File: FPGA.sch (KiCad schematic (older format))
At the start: 32 parts, among them P3 CONN_02X22, P4 CONN_02X22, SW1 SW_PUSH, U6 ICE40HX1K-VQ100, X2 IQXO/7X

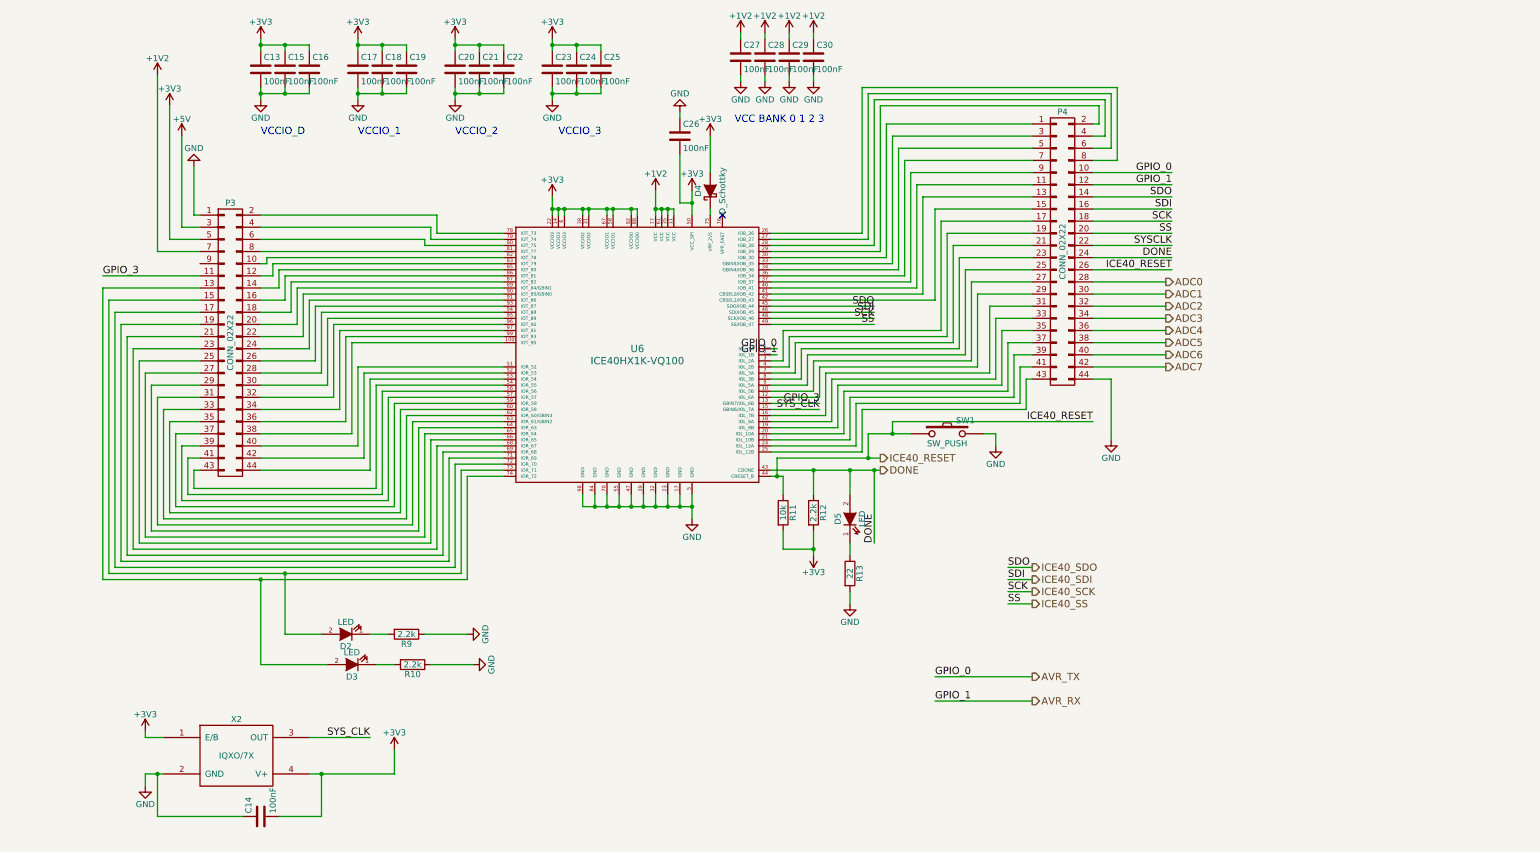
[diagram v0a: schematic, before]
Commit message: Redesign FPGA <-> connectors
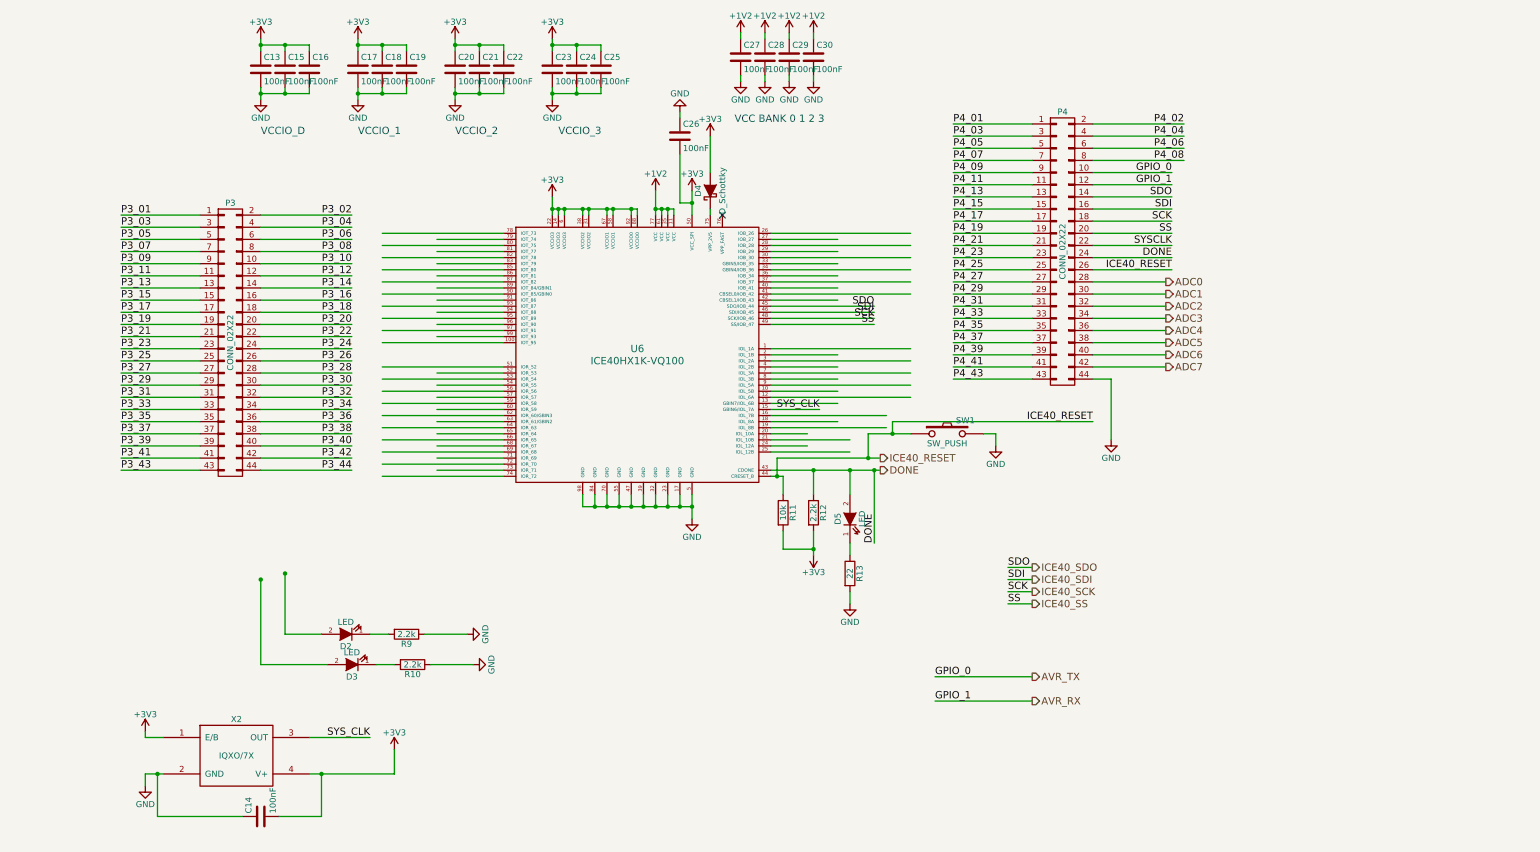
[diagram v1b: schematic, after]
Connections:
- net labels added: P3_01, P3_02, P3_03, P3_04, P3_05, P3_06, P3_07, P3_08, P3_09, P3_10, P3_11, P3_12, P3_13, P3_14, P3_15, P3_16, P3_17, P3_18, P3_19, P3_20, P3_21, P3_22, P3_23, P3_24, P3_25, P3_26, P3_27, P3_28, P3_29, P3_30, P3_31, P3_32, P3_33, P3_34, P3_35, P3_36, P3_37, P3_38, P3_39, P3_40, P3_41, P3_42, P3_43, P3_44, P4_01, P4_02, P4_03, P4_04, P4_05, P4_06, P4_07, P4_08, P4_09, P4_11, P4_13, P4_15, P4_17, P4_19, P4_21, P4_23, P4_25, P4_27, P4_29, P4_31, P4_33, P4_35, P4_37, P4_39, P4_41, P4_43
- net labels removed: +5V, GPIO_3
- wire segments 411 -> 278

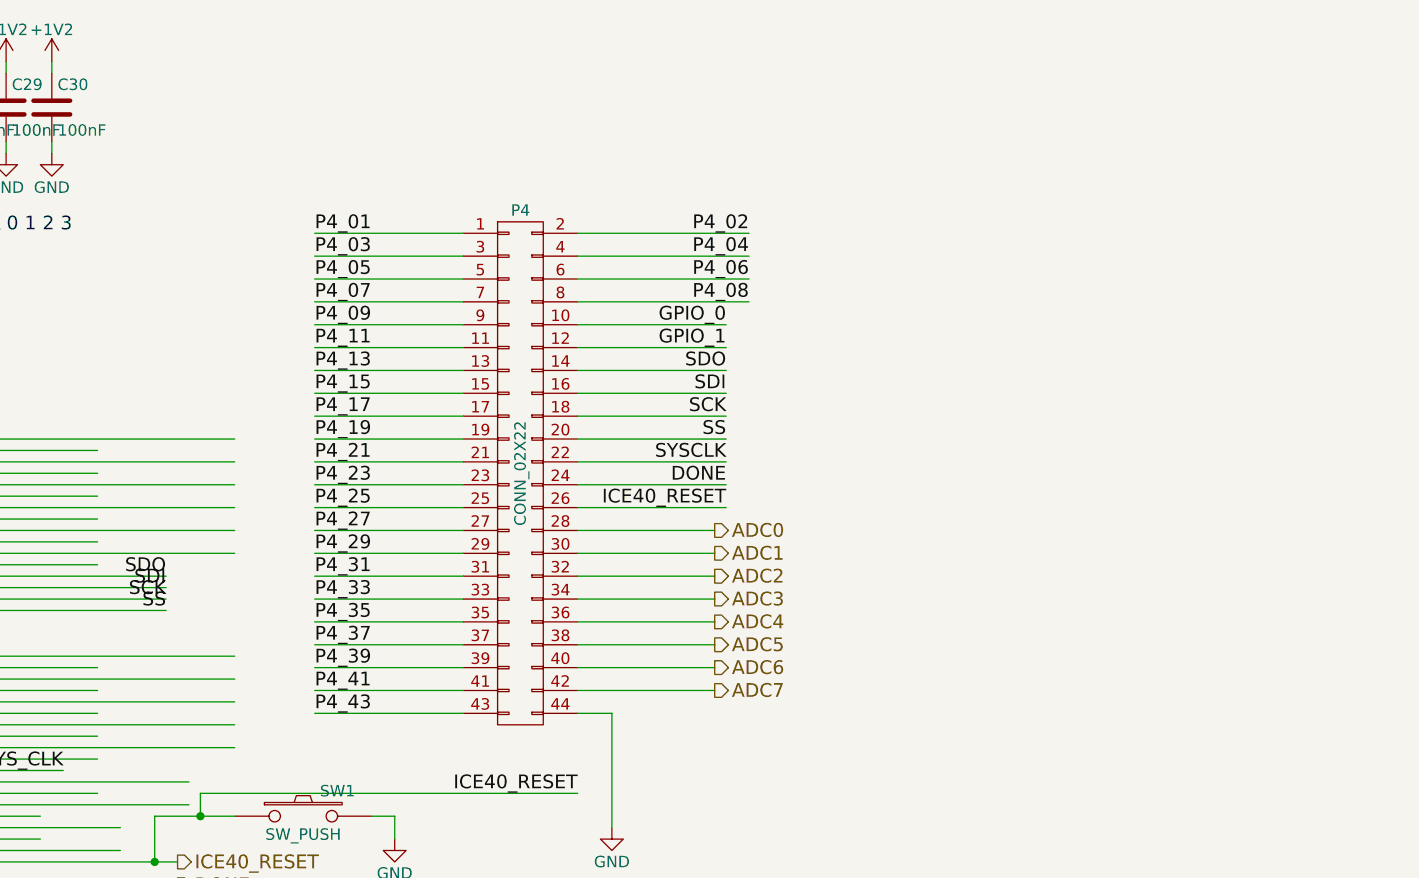
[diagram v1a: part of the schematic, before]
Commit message: Reorder conectors <-> FPGA
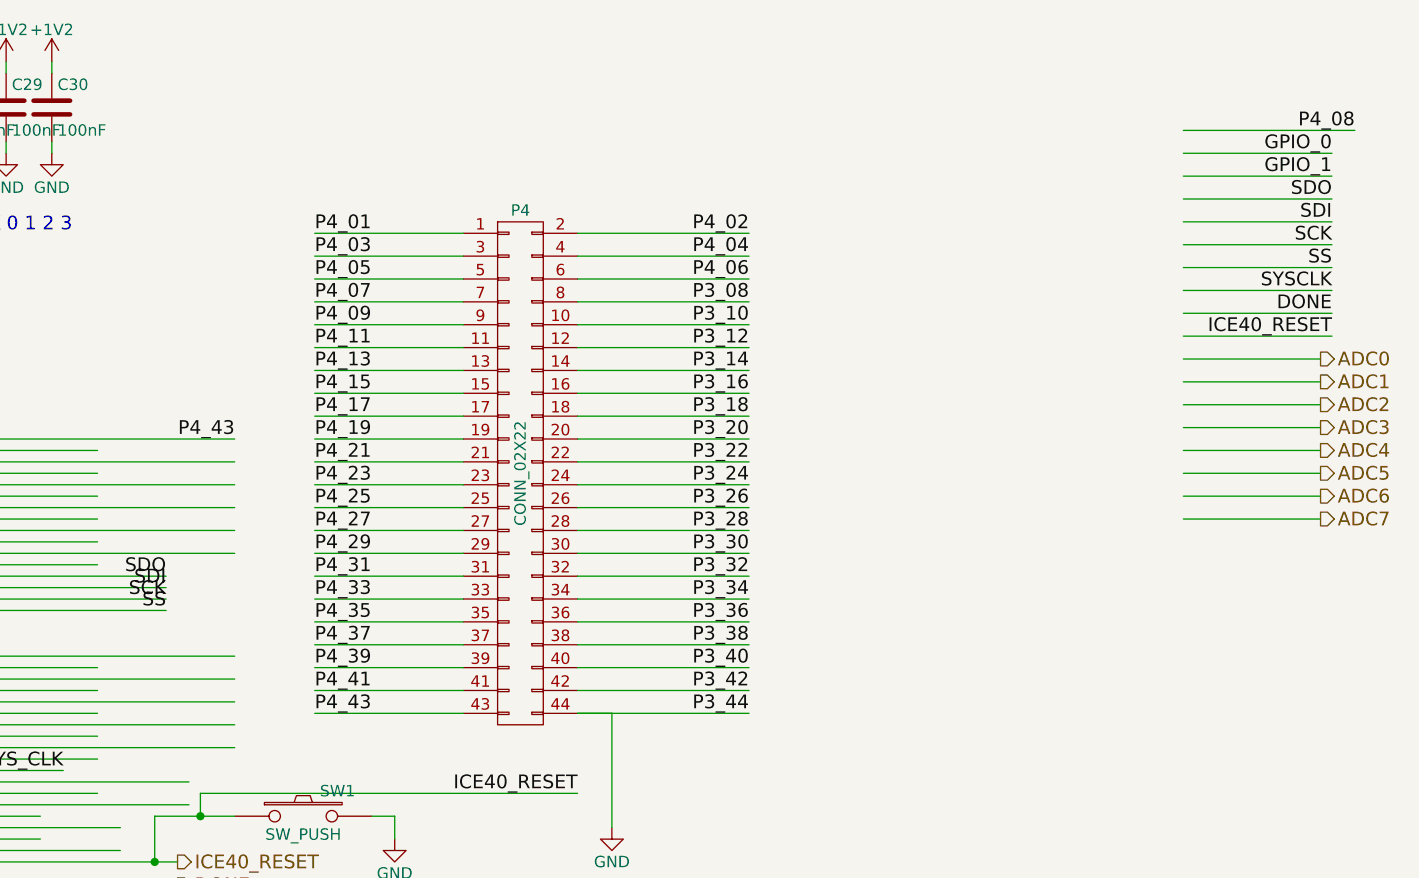
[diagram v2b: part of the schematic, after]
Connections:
- wire segments 278 -> 297
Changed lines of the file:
@@
 	7050 3850 7450 3850
 Wire Wire Line
-	9700 1900 10350 1900
-Wire Wire Line
-	9700 2000 10350 2000
-Text Label 10350 1900 2    60   ~ 0
+	12350 1150 13000 1150
+Wire Wire Line
+	12350 1250 13000 1250
+Text Label 13000 1150 2    60   ~ 0
 GPIO_0
-Text Label 10350 2000 2    60   ~ 0
+Text Label 13000 1250 2    60   ~ 0
 GPIO_1
 Wire Wire Line
@@
 SS
 Wire Wire Line
-	9700 2100 10350 2100
-Wire Wire Line
-	9700 2200 10350 2200
-Wire Wire Line
-	9700 2300 10350 2300
-Wire Wire Line
-	9700 2400 10350 2400
-Text Label 10350 2100 2    60   ~ 0
+	12350 1350 13000 1350
+Wire Wire Line
+	12350 1450 13000 1450
+Wire Wire Line
+	12350 1550 13000 1550
+Wire Wire Line
+	12350 1650 13000 1650
+Text Label 13000 1350 2    60   ~ 0
 SDO
-Text Label 10350 2200 2    60   ~ 0
+Text Label 13000 1450 2    60   ~ 0
 SDI
-Text Label 10350 2300 2    60   ~ 0
+Text Label 13000 1550 2    60   ~ 0
 SCK
-Text Label 10350 2400 2    60   ~ 0
+Text Label 13000 1650 2    60   ~ 0
 SS
 Wire Wire Line
-	9700 2500 10350 2500
-Text Label 10350 2500 2    60   ~ 0
+	12350 1750 13000 1750
+Text Label 13000 1750 2    60   ~ 0
 SYSCLK
 Wire Wire Line
@@
 DONE
 Wire Wire Line
-	9700 2600 10350 2600
-Text Label 10350 2600 2    60   ~ 0
+	12350 1850 13000 1850
+Text Label 13000 1850 2    60   ~ 0
 DONE
 Wire Wire Line
@@
 ICE40_RESET
 Wire Wire Line
-	9700 2700 10350 2700
-Text Label 10350 2700 2    60   ~ 0
+	12350 1950 13000 1950
+Text Label 13000 1950 2    60   ~ 0
 ICE40_RESET
 Wire Wire Line
@@
 $EndComp
 Wire Wire Line
-	9700 2800 10300 2800
-Wire Wire Line
-	9700 2900 10300 2900
-Wire Wire Line
-	9700 3000 10300 3000
-Wire Wire Line
-	9700 3100 10300 3100
-Wire Wire Line
-	9700 3200 10300 3200
-Wire Wire Line
-	9700 3300 10300 3300
-Wire Wire Line
-	9700 3400 10300 3400
-Wire Wire Line
-	9700 3500 10300 3500
-Text HLabel 10300 2800 2    60   Output ~ 0
+	12350 2050 12950 2050
+Wire Wire Line
+	12350 2150 12950 2150
+Wire Wire Line
+	12350 2250 12950 2250
+Wire Wire Line
+	12350 2350 12950 2350
+Wire Wire Line
+	12350 2450 12950 2450
+Wire Wire Line
+	12350 2550 12950 2550
+Wire Wire Line
+	12350 2650 12950 2650
+Wire Wire Line
+	12350 2750 12950 2750
+Text HLabel 12950 2050 2    60   Output ~ 0
 ADC0
-Text HLabel 10300 2900 2    60   Output ~ 0
+Text HLabel 12950 2150 2    60   Output ~ 0
 ADC1
-Text HLabel 10300 3000 2    60   Output ~ 0
+Text HLabel 12950 2250 2    60   Output ~ 0
 ADC2
-Text HLabel 10300 3100 2    60   Output ~ 0
+Text HLabel 12950 2350 2    60   Output ~ 0
 ADC3
-Text HLabel 10300 3200 2    60   Output ~ 0
+Text HLabel 12950 2450 2    60   Output ~ 0
 ADC4
-Text HLabel 10300 3300 2    60   Output ~ 0
+Text HLabel 12950 2550 2    60   Output ~ 0
 ADC5
-Text HLabel 10300 3400 2    60   Output ~ 0
+Text HLabel 12950 2650 2    60   Output ~ 0
 ADC6
-Text HLabel 10300 3500 2    60   Output ~ 0
+Text HLabel 12950 2750 2    60   Output ~ 0
 ADC7
 $Comp
@@
 Text Label 10450 1700 2    60   ~ 0
 P4_06
-Text Label 10450 1800 2    60   ~ 0
+Text Label 13100 1050 2    60   ~ 0
 P4_08
 Wire Wire Line
-	9700 1800 10450 1800
+	12350 1050 13100 1050
 Wire Wire Line
 	2350 2250 1700 2250
@@
 Wire Wire Line
 	7050 4200 7700 4200
+Text Label 8200 2400 2    60   ~ 0
+P4_43
+Wire Wire Line
+	9700 1800 10450 1800
+Text Label 10450 1800 2    60   ~ 0
+P3_08
+Wire Wire Line
+	9700 1900 10450 1900
+Text Label 10450 1900 2    60   ~ 0
+P3_10
+Wire Wire Line
+	9700 2000 10450 2000
+Text Label 10450 2000 2    60   ~ 0
+P3_12
+Wire Wire Line
+	9700 2100 10450 2100
+Text Label 10450 2100 2    60   ~ 0
+P3_14
+Wire Wire Line
+	9700 2300 10450 2300
+Text Label 10450 2300 2    60   ~ 0
+P3_18
+Wire Wire Line
+	9700 2400 10450 2400
+Text Label 10450 2400 2    60   ~ 0
+P3_20
+Wire Wire Line
+	9700 2500 10450 2500
+Text Label 10450 2500 2    60   ~ 0
+P3_22
+Wire Wire Line
+	9700 2600 10450 2600
+Text Label 10450 2600 2    60   ~ 0
+P3_24
+Wire Wire Line
+	9700 2700 10450 2700
+Text Label 10450 2700 2    60   ~ 0
+P3_26
+Wire Wire Line
+	9700 2800 10450 2800
+Text Label 10450 2800 2    60   ~ 0
+P3_28
+Wire Wire Line
+	9700 2900 10450 2900
+Text Label 10450 2900 2    60   ~ 0
+P3_30
+Wire Wire Line
+	9700 3100 10450 3100
+Text Label 10450 3100 2    60   ~ 0
+P3_34
+Wire Wire Line
+	9700 3200 10450 3200
+Text Label 10450 3200 2    60   ~ 0
+P3_36
+Wire Wire Line
+	9700 3300 10450 3300
+Text Label 10450 3300 2    60   ~ 0
+P3_38
+Wire Wire Line
+	9700 3400 10450 3400
+Text Label 10450 3400 2    60   ~ 0
+P3_40
+Wire Wire Line
+	9700 3500 10450 3500
+Text Label 10450 3500 2    60   ~ 0
+P3_42
+Wire Wire Line
+	9700 3600 10450 3600
+Text Label 10450 3600 2    60   ~ 0
+P3_44
+Wire Wire Line
+	9700 2200 10450 2200
+Text Label 10450 2200 2    60   ~ 0
+P3_16
+Wire Wire Line
+	9700 3000 10450 3000
+Text Label 10450 3000 2    60   ~ 0
+P3_32
 $EndSCHEMATC

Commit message: Change in PCB with new connections
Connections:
- net labels added: +5V, P4_10, P4_12, P4_14, P4_16, P4_18, P4_20, P4_22, P4_24, P4_26, P4_28, P4_30, P4_32, P4_34, P4_36, P4_38, P4_40, P4_42, P4_44
- net labels removed: GPIO_0, GPIO_1, SYSCLK
- wire segments 297 -> 296
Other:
- moved on the sheet: C14, D2, D3, R10, R9, X2

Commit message: Connect all pads and edge cuts
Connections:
- net ICE40_RESET: no longer P4.3 (P3)
- net P4_19: no longer U6.66 (IOR_65)
- new net P4_03: P4.3 (P3)
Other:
- note added: "P4_03 for ice reset\n"
- note added: "P4_19 on pin 66\n"
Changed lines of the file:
@@
 Text Label 3850 4000 0    60   ~ 0
 P4_21
-Text Label 3850 4100 0    60   ~ 0
-P4_19
 Text Label 3850 4200 0    60   ~ 0
 P4_17
@@
 Text Label 5250 6450 0    60   ~ 0
 P4_01
-Text Label 5250 6550 0    60   ~ 0
-P4_03
 Text Label 5250 6650 0    60   ~ 0
 P4_05
@@
 	1    0    0    -1
 $EndComp
+Text Notes 3850 4550 0    60   ~ 0
+P4_19 on pin 66\n
+Text Notes 4000 6600 0    60   ~ 0
+P4_03 for  ice reset\n
 $EndSCHEMATC
